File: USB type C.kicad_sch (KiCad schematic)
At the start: 7 parts, among them J10 USB_C_Receptacle, U9 USBLC6-2SC6

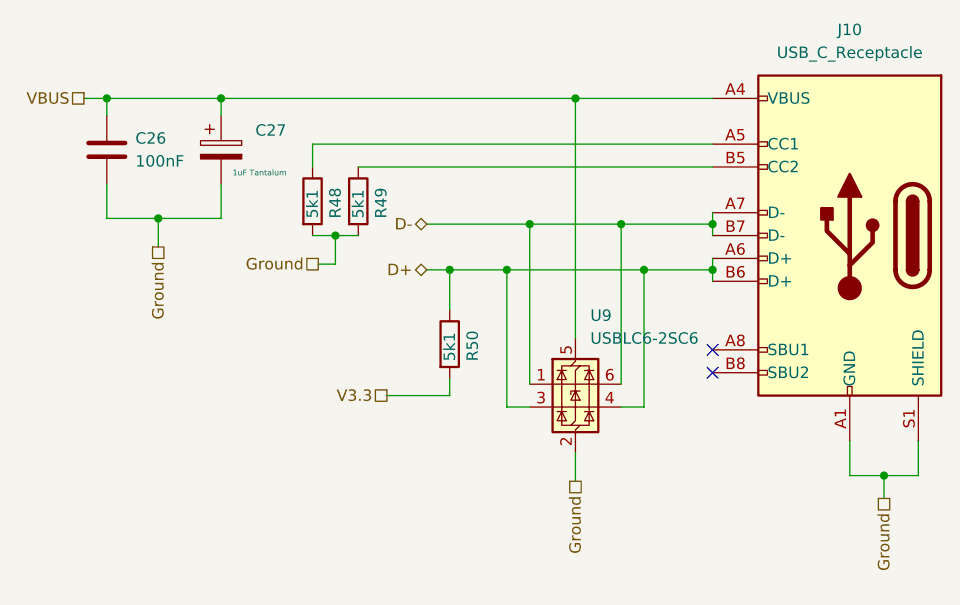
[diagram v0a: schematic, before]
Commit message: Add LORA, SDcard and Volt to 4_20mA scheamtic
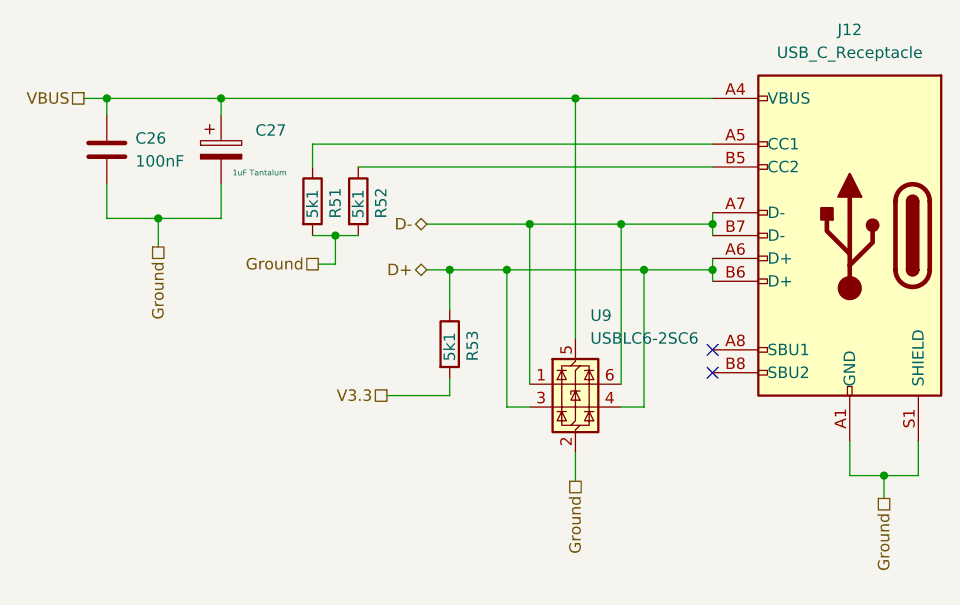
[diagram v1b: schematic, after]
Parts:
- renumbered J10 to J12, R48 to R51, R49 to R52, R50 to R53
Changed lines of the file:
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@@
 		(on_board yes)
 		(dnp no)
-		(property "Reference" "R49"
+		(property "Reference" "R52"
 			(at 76.2 83.82 90)
 			(effects
@@
 			(project "DongTamV2"
 				(path "/2303d546-b88a-4ab0-aee1-26e3b32ac9d7/dea6fb52-48af-4515-b6f6-569a8035386e"
-					(reference "R49")
+					(reference "R52")
 					(unit 1)
 				)
@@
 		(on_board yes)
 		(dnp no)
-		(property "Reference" "J10"
+		(property "Reference" "J12"
 			(at 128.27 62.865 0)
 			(effects
@@
 			(project "DongTamV2"
 				(path "/2303d546-b88a-4ab0-aee1-26e3b32ac9d7/dea6fb52-48af-4515-b6f6-569a8035386e"
-					(reference "J10")
+					(reference "J12")
 					(unit 1)
 				)
@@
 		(on_board yes)
 		(dnp no)
-		(property "Reference" "R48"
+		(property "Reference" "R51"
 			(at 71.12 83.82 90)
 			(effects
@@
 			(project "DongTamV2"
 				(path "/2303d546-b88a-4ab0-aee1-26e3b32ac9d7/dea6fb52-48af-4515-b6f6-569a8035386e"
-					(reference "R48")
+					(reference "R51")
 					(unit 1)
 				)
@@
 		(on_board yes)
 		(dnp no)
-		(property "Reference" "R50"
+		(property "Reference" "R53"
 			(at 86.36 99.695 90)
 			(effects
@@
 			(project "DongTamV2"
 				(path "/2303d546-b88a-4ab0-aee1-26e3b32ac9d7/dea6fb52-48af-4515-b6f6-569a8035386e"
-					(reference "R50")
-					(unit 1)
-				)
+					(reference "R53")
+					(unit 1)
+				)

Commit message: layout p1
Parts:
- R53: value 5k1 -> 1k5
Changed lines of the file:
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@@
 			)
 		)
-		(property "Value" "5k1"
+		(property "Value" "1k5"
 			(at 83.82 99.695 90)
 			(effects
